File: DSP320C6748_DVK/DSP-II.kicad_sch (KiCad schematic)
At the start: 1 part, among them U1 TMS320C6748EZWT4

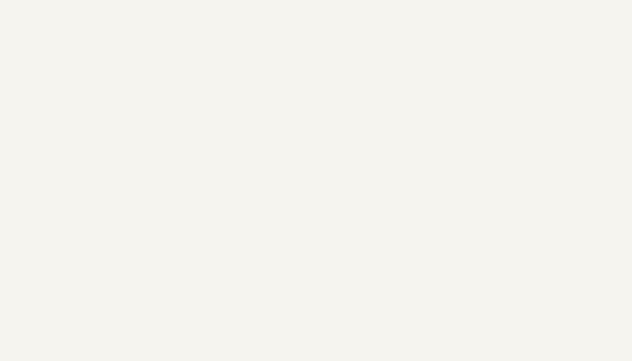
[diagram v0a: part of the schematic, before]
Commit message: TPS650250 Section Added
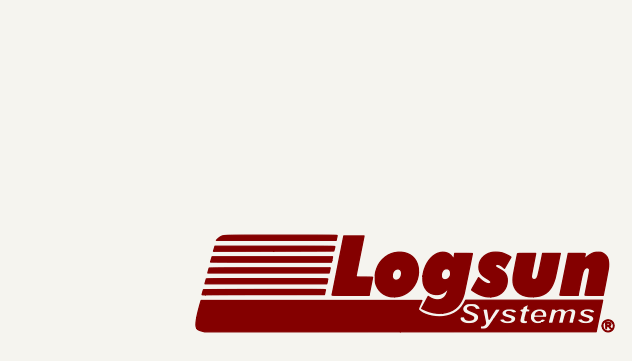
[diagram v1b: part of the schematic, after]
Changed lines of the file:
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@@
+		)
+	)
+	(symbol
+		(lib_id "Logsun_Logo:LOGO")
+		(at 260.35 173.99 0)
+		(unit 1)
+		(exclude_from_sim no)
+		(in_bom yes)
+		(on_board yes)
+		(dnp no)
+		(fields_autoplaced yes)
+		(property "Reference" "#G4"
+			(at 260.35 168.025 0)
+			(effects
+				(font
+					(size 1.27 1.27)
+				)
+				(hide yes)
+			)
+		)
+		(property "Value" "LOGO"
+			(at 260.35 179.955 0)
+			(effects
+				(font
+					(size 1.27 1.27)
+				)
+				(hide yes)
+			)
+		)
+		(property "Footprint" ""
+			(at 260.35 173.99 0)
+			(effects
+				(font
+					(size 1.27 1.27)
+				)
+				(hide yes)
+			)
+		)
+		(property "Datasheet" ""
+			(at 260.35 173.99 0)
+			(effects
+				(font
+					(size 1.27 1.27)
+				)
+				(hide yes)
+			)
+		)
+		(property "Description" ""
+			(at 260.35 173.99 0)
+			(effects
+				(font
+					(size 1.27 1.27)
+				)
+				(hide yes)
+			)
+		)
+		(instances
+			(project "DSP320C6748_DVK"
+				(path "/3a70ffc0-9fe7-4a5b-b3c2-23140355df82/2c62b8f0-d70b-43f3-91ef-f5cb46303462"
+					(reference "#G4")
+					(unit 1)
+				)
+			)
 		)
 	)

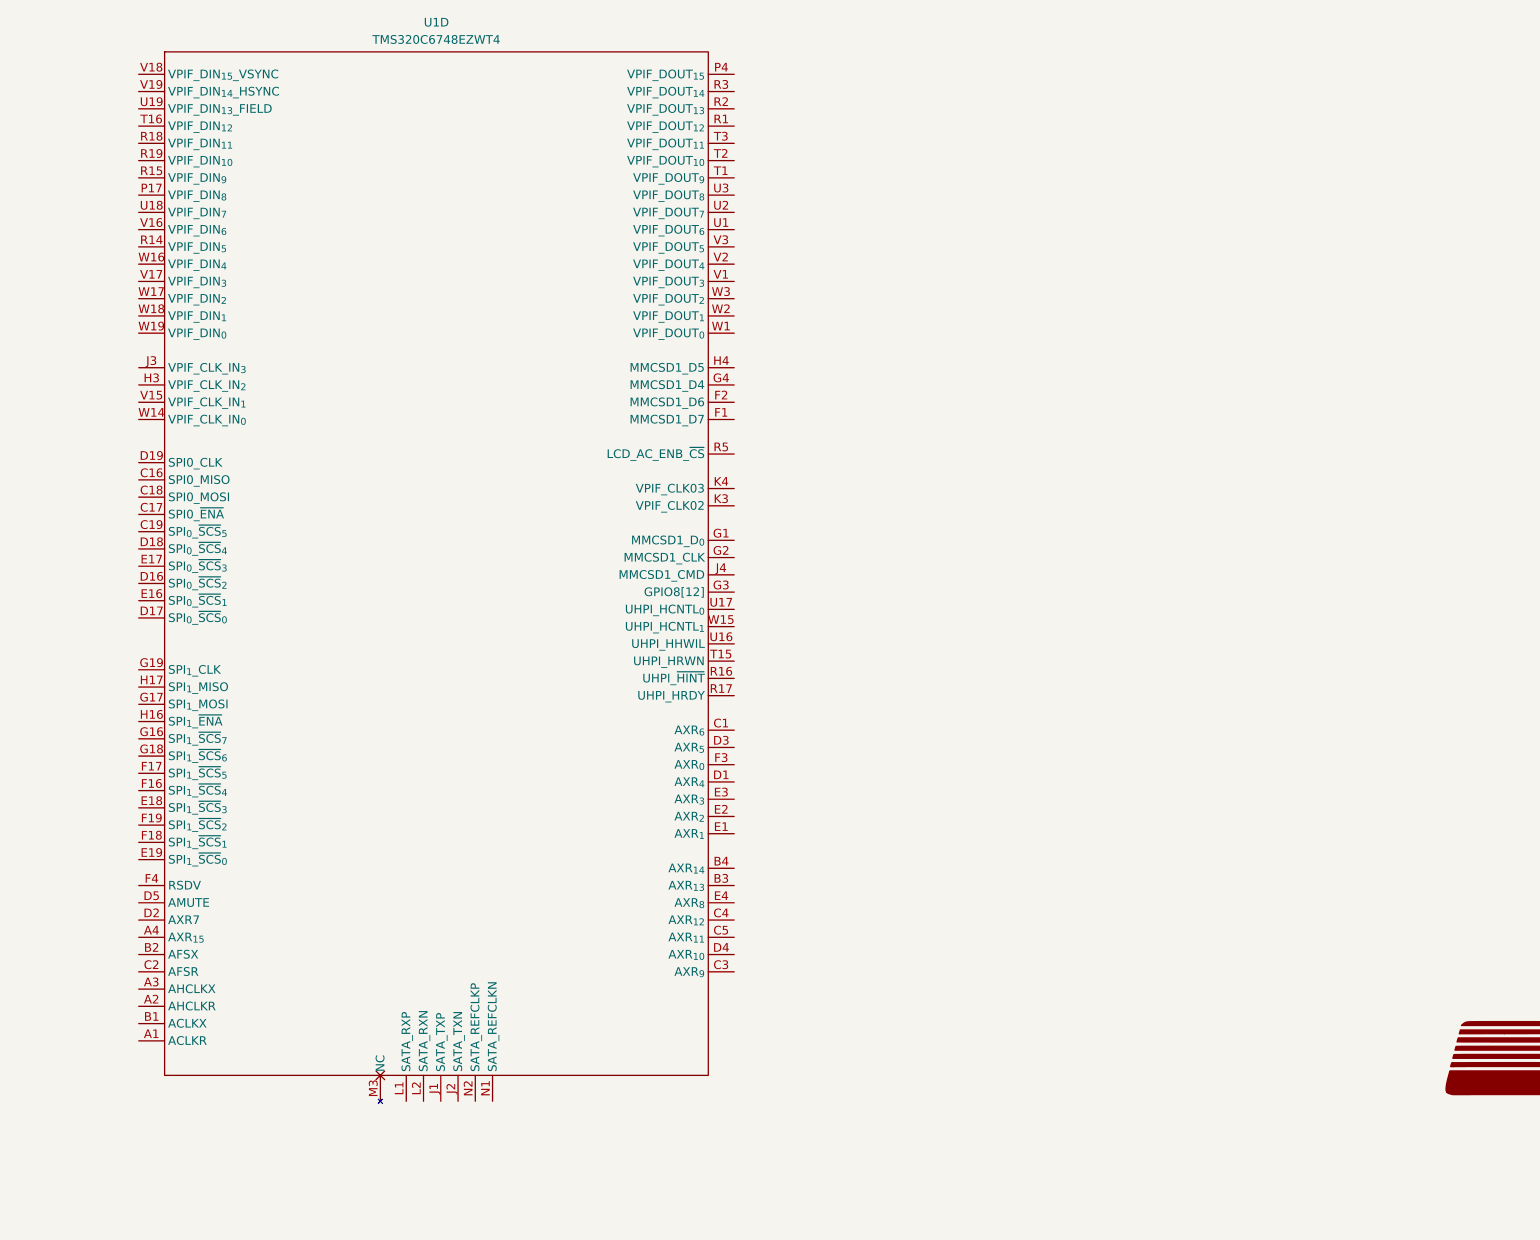
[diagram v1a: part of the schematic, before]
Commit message: Serial Circuit completed, SATA section Added, DSP Reset Section Added
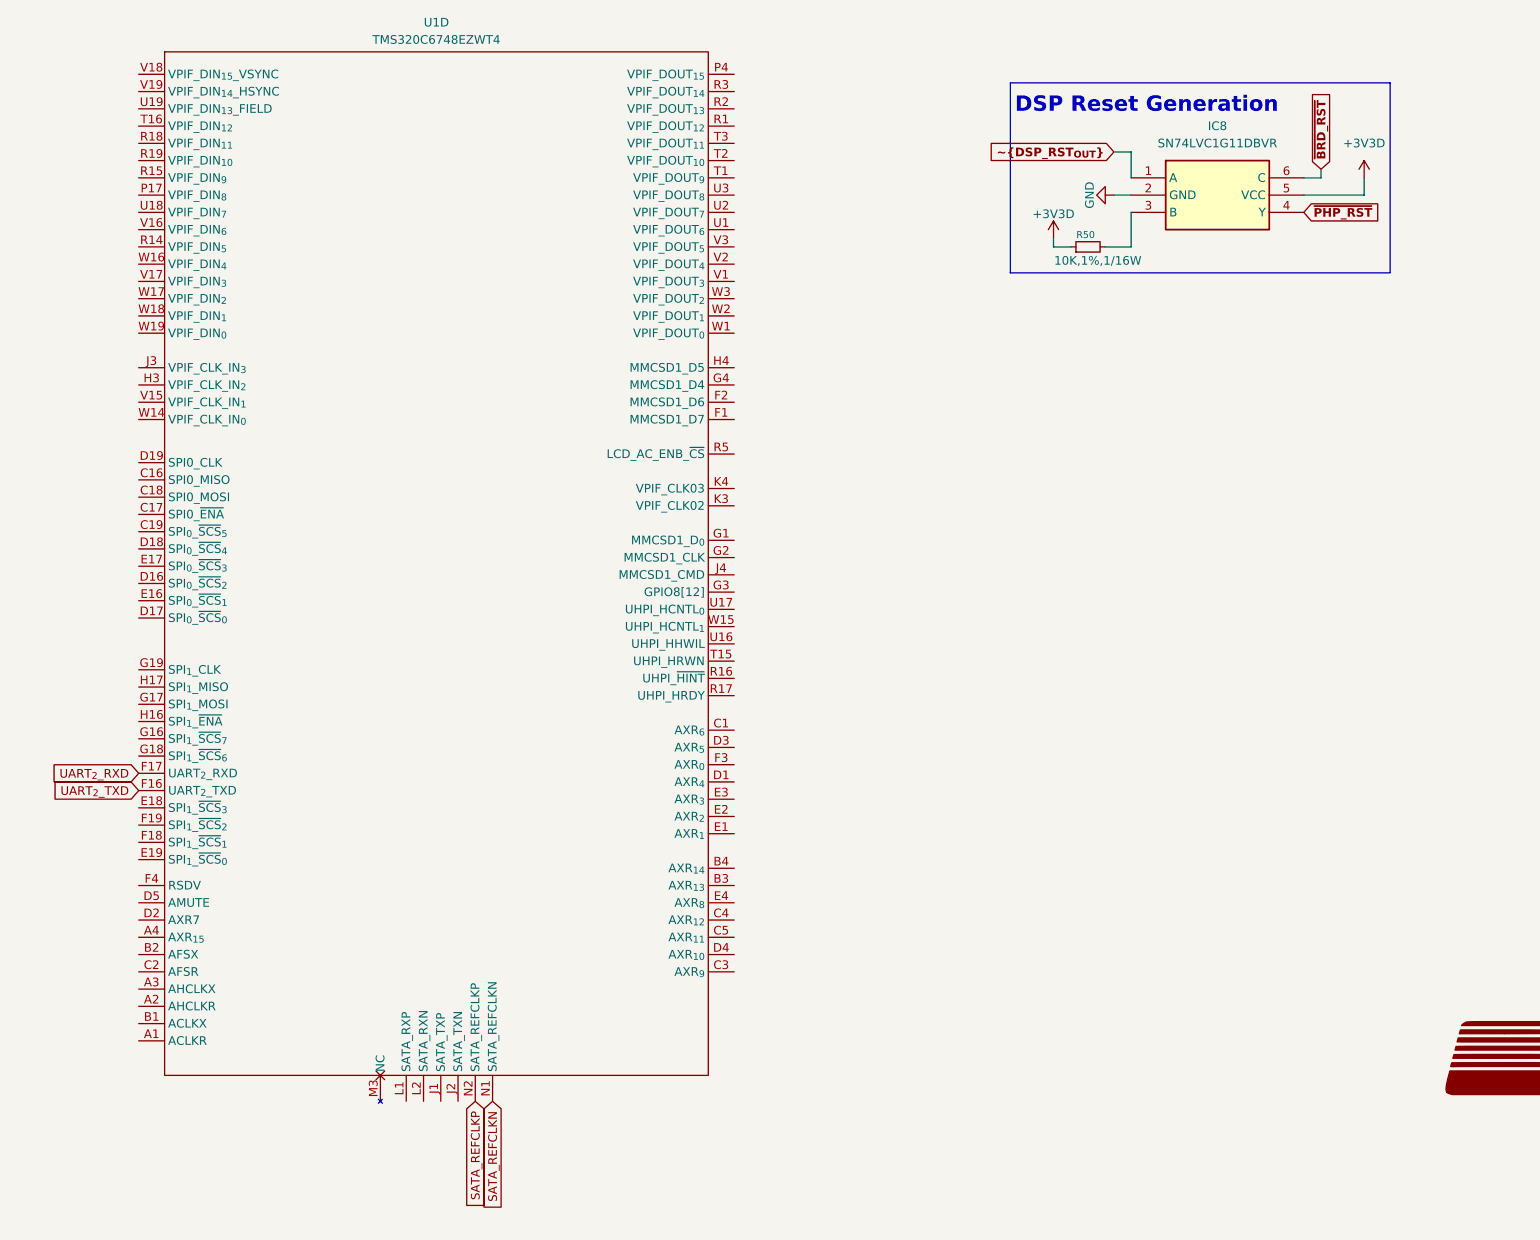
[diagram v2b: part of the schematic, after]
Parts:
- added IC8: SN74LVC1G11DBVR, SOT95P280X145-6N, symbol SN74LVC1G11DBVR:SN74LVC1G11DBVR
- added R50: 10K,1%,1/16W, symbol Device:R_Small
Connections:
- net UART_{2}_TXD: now reaches U1.F16 (SPI_{1}_~{SCS}_{4})
- net UART_{2}_RXD: now reaches U1.F17 (SPI_{1}_~{SCS}_{5})
- net SATA_REFCLKN: now reaches U1.N1 (SATA_REFCLKN)
- net SATA_REFCLKP: now reaches U1.N2 (SATA_REFCLKP)
- new net: IC8.3 (B), R50.2
- new net +3V3D: IC8.5 (VCC), R50.1
- new net GND: IC8.2 (GND)
- new net ~{BRD_RST}: IC8.6 (C)
- new net ~{DSP_RST_{OUT}}: IC8.1 (A)
- new net ~{PHP_RST}: IC8.4 (Y)
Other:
- note added: "DSP Reset Generation"
